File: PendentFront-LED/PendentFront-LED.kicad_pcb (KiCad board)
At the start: 2 copper layers, 26.7 x 39.2 mm, 95 parts, among them J1 Conn_01x03_Pin, J2 Conn_01x02_Pin, U1 74VHC9595FT, U2 74VHC9595FT, U3 74VHC9595FT, U4 74VHC9595FT

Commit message: Nearly done with routing
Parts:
- moved J2 7.83 mm to (105.2, 82.4), turned to 45 degrees
- moved C1 7.11 mm to (104.3, 75.5), turned to -90 degrees
- moved R23 3.23 mm to (115.0, 83.8), turned to 90 degrees
- moved J1 0.56 mm to (107.3, 83.9), turned to -112.5 degrees
- moved R11 0.51 mm to (121.0, 64.2)
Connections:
- U1 pad 10: /ROW5 -> /ROW1
- U1 pad 11: /ROW6 -> /ROW2
- U1 pad 12: /ROW7 -> /ROW3
- U1 pad 13: /ROW8 -> /ROW4
- U1 pad 5: /ROW1 -> /ROW8
- U1 pad 6: /ROW2 -> /ROW7
- U1 pad 7: /ROW3 -> /ROW6
- U1 pad 9: /ROW4 -> /ROW5
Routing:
- net /ROW5: track 0.00 -> 136.7 mm, vias 0 -> 21
- net /ROW6: track 0.00 -> 111.4 mm, vias 0 -> 19
- net /ROW7: track 0.00 -> 103.2 mm, vias 0 -> 20
- net /ROW8: track 0.00 -> 75.0 mm, vias 0 -> 8
- net /ROW4: track 65.4 -> 127.2 mm, vias 10 -> 21
- net /ROW2: track 45.1 -> 105.8 mm, vias 8 -> 16
- net /ROW3: track 52.2 -> 108.3 mm, vias 12 -> 24
- net /ROW1: track 35.4 -> 83.6 mm, vias 10 -> 18
- net VCC: track 12.6 -> 49.0 mm, vias 0 -> 4
- net Net-(U2-Q8C): track 0.00 -> 23.6 mm, vias 0 -> 2
- net CLK: track 10.5 -> 30.8 mm, vias 0 -> 4
- net RCK: track 10.9 -> 31.0 mm, vias 0 -> 4
- net Net-(U3-Q8C): track 0.00 -> 14.8 mm
- net GND: track 0.00 -> 13.7 mm, vias 0 -> 2
- net SerialIn: track 11.2 -> 0.00 mm
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
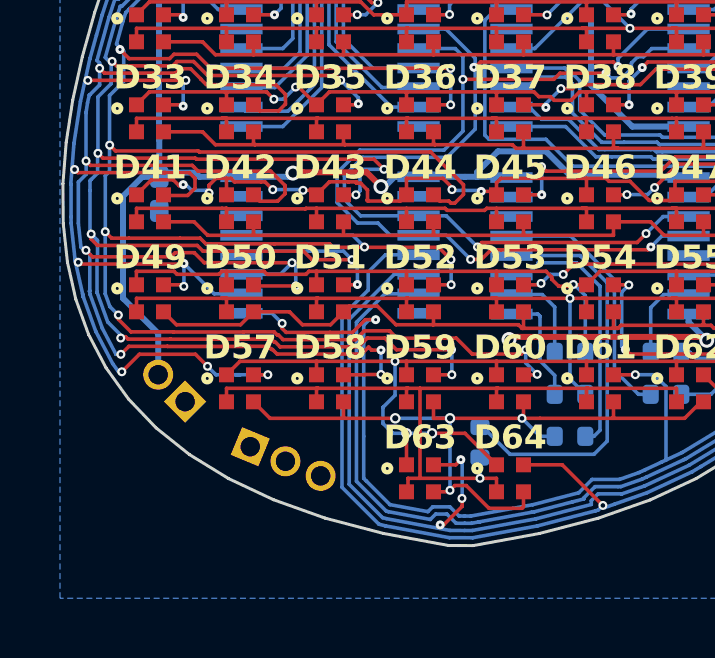
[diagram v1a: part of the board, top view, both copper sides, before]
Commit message: Tried to get CTRL inputs to get connected - needs some squeezing
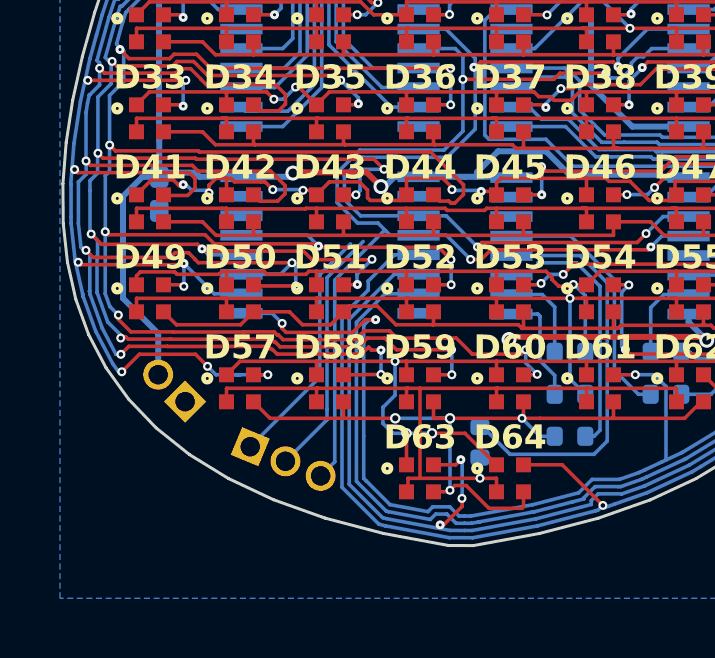
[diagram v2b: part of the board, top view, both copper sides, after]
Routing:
- net CLK: track 30.8 -> 39.9 mm
- net RCK: track 31.0 -> 39.4 mm
- net SerialIn: track 0.00 -> 8.15 mm
- net /ROW4: track 127.2 -> 125.7 mm
- net /ROW3: track 108.3 -> 106.8 mm, vias 24 -> 25
